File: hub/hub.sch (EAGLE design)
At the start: 5 parts

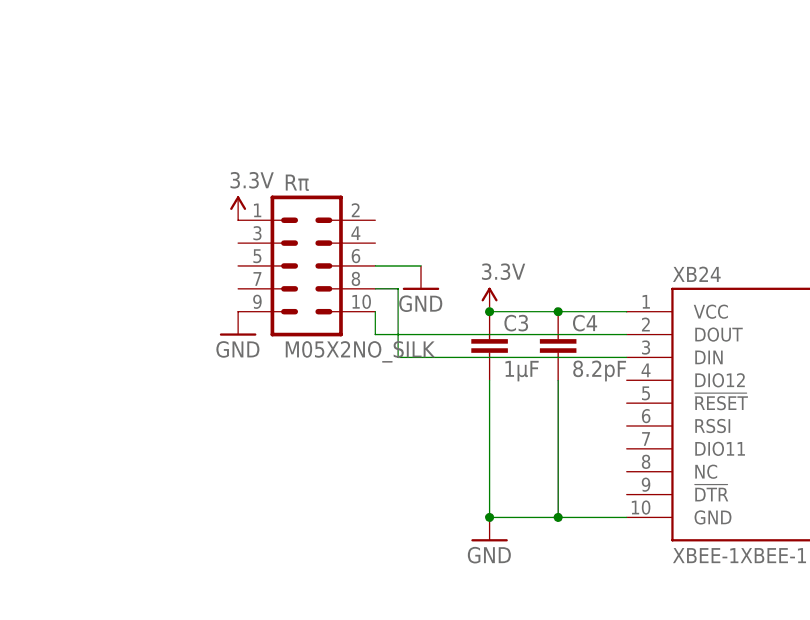
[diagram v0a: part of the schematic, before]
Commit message: use the largest header we can fit, for stability and to look cool?
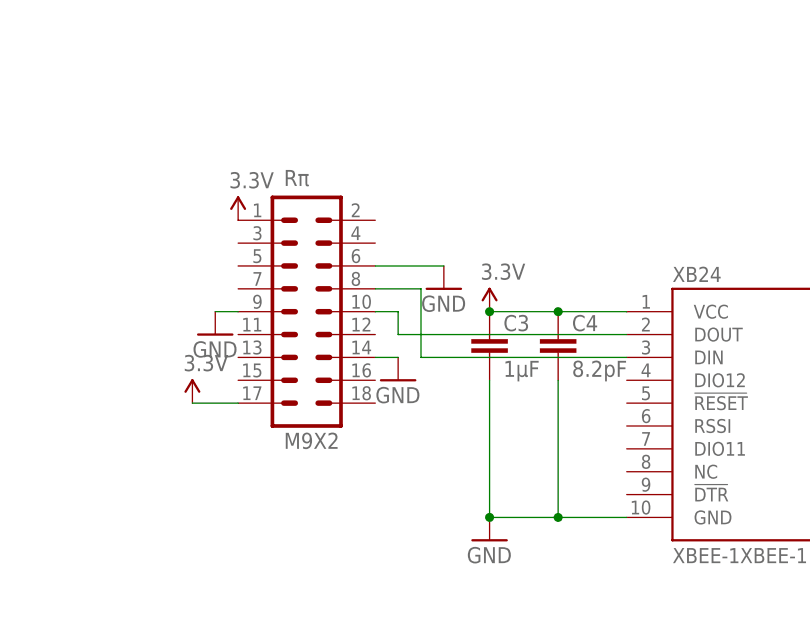
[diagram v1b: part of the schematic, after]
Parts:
- Rπ: value M05X2NO_SILK -> M9X2; device SparkFun-Connectors:M05X2NO_SILK -> hrldcpr:M9X2
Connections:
- net 3.3V: now also Rπ.17
- net GND: now also Rπ.14
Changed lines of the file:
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@@
 <part name="FRAME1" library="SparkFun-Aesthetics" deviceset="FRAME-LETTER" device=""/>
 <part name="XB24" library="hrldcpr" deviceset="XBEE-1" device="XBEE-1"/>
-<part name="Rπ" library="SparkFun-Connectors" deviceset="M05X2" device="NO_SILK"/>
+<part name="Rπ" library="hrldcpr" deviceset="M9X2" device=""/>
 <part name="SUPPLY1" library="SparkFun-Aesthetics" deviceset="3.3V" device=""/>
 <part name="GND1" library="SparkFun-Aesthetics" deviceset="GND" device=""/>
@@
 <part name="C3" library="SparkFun-Capacitors" deviceset="CAP" device="0805" value="1µF"/>
 <part name="C4" library="SparkFun-Capacitors" deviceset="CAP" device="0805" value="8.2pF"/>
+<part name="GND3" library="SparkFun-Aesthetics" deviceset="GND" device=""/>
+<part name="SUPPLY2" library="SparkFun-Aesthetics" deviceset="3.3V" device=""/>
 </parts>
 <sheets>
@@
 <instance part="FRAME1" gate="G$2" x="147.32" y="0"/>
 <instance part="XB24" gate="G$1" x="119.38" y="101.6"/>
-<instance part="Rπ" gate="G$1" x="63.5" y="116.84"/>
+<instance part="Rπ" gate="G$1" x="63.5" y="111.76"/>
 <instance part="SUPPLY1" gate="G$1" x="55.88" y="121.92"/>
-<instance part="GND1" gate="1" x="55.88" y="109.22"/>
-<instance part="GND2" gate="1" x="76.2" y="114.3"/>
+<instance part="GND1" gate="1" x="53.34" y="109.22"/>
+<instance part="GND2" gate="1" x="78.74" y="114.3"/>
 <instance part="SUPPLY3" gate="G$1" x="83.82" y="111.76"/>
 <instance part="GND4" gate="1" x="83.82" y="86.36"/>
 <instance part="C3" gate="G$1" x="83.82" y="106.68"/>
 <instance part="C4" gate="G$1" x="91.44" y="106.68"/>
+<instance part="GND3" gate="1" x="73.66" y="104.14"/>
+<instance part="SUPPLY2" gate="G$1" x="50.8" y="101.6"/>
 </instances>
 <busses>
@@
 <pinref part="XB24" gate="G$1" pin="VCC"/>
 </segment>
+<segment>
+<pinref part="Rπ" gate="G$1" pin="17"/>
+<pinref part="SUPPLY2" gate="G$1" pin="3.3V"/>
+<wire x1="50.8" y1="101.6" x2="55.88" y2="101.6" width="0.1524" layer="91"/>
+</segment>
 </net>
 <net name="GND" class="0">
@@
 <pinref part="Rπ" gate="G$1" pin="9"/>
 <pinref part="GND1" gate="1" pin="GND"/>
+<wire x1="53.34" y1="111.76" x2="55.88" y2="111.76" width="0.1524" layer="91"/>
 </segment>
 <segment>
 <pinref part="Rπ" gate="G$1" pin="6"/>
 <pinref part="GND2" gate="1" pin="GND"/>
-<wire x1="71.12" y1="116.84" x2="76.2" y2="116.84" width="0.1524" layer="91"/>
+<wire x1="71.12" y1="116.84" x2="78.74" y2="116.84" width="0.1524" layer="91"/>
 </segment>
 <segment>
@@
 <pinref part="XB24" gate="G$1" pin="GND"/>
 </segment>
+<segment>
+<pinref part="Rπ" gate="G$1" pin="14"/>
+<pinref part="GND3" gate="1" pin="GND"/>
+<wire x1="73.66" y1="106.68" x2="71.12" y2="106.68" width="0.1524" layer="91"/>
+</segment>
 </net>
 <net name="N$2" class="0">
 <segment>
 <pinref part="Rπ" gate="G$1" pin="8"/>
-<wire x1="71.12" y1="114.3" x2="73.66" y2="114.3" width="0.1524" layer="91"/>
-<wire x1="73.66" y1="114.3" x2="73.66" y2="106.68" width="0.1524" layer="91"/>
+<wire x1="71.12" y1="114.3" x2="76.2" y2="114.3" width="0.1524" layer="91"/>
+<wire x1="76.2" y1="114.3" x2="76.2" y2="106.68" width="0.1524" layer="91"/>
 <pinref part="XB24" gate="G$1" pin="DIN"/>
-<wire x1="73.66" y1="106.68" x2="99.06" y2="106.68" width="0.1524" layer="91"/>
+<wire x1="76.2" y1="106.68" x2="99.06" y2="106.68" width="0.1524" layer="91"/>
 </segment>
 </net>
 <net name="N$1" class="0">
 <segment>
+<pinref part="XB24" gate="G$1" pin="DOUT"/>
+<wire x1="73.66" y1="109.22" x2="99.06" y2="109.22" width="0.1524" layer="91"/>
 <pinref part="Rπ" gate="G$1" pin="10"/>
-<wire x1="71.12" y1="111.76" x2="71.12" y2="109.22" width="0.1524" layer="91"/>
-<pinref part="XB24" gate="G$1" pin="DOUT"/>
-<wire x1="71.12" y1="109.22" x2="99.06" y2="109.22" width="0.1524" layer="91"/>
+<wire x1="71.12" y1="111.76" x2="73.66" y2="111.76" width="0.1524" layer="91"/>
+<wire x1="73.66" y1="111.76" x2="73.66" y2="109.22" width="0.1524" layer="91"/>
 </segment>
 </net>
